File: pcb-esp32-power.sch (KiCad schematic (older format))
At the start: 15 parts, among them IC2 SY8008B, J1 C-OBD-II-16M, J2 Conn_01x02, J3 Bus_Connector, U1 STEPDOWN12_5

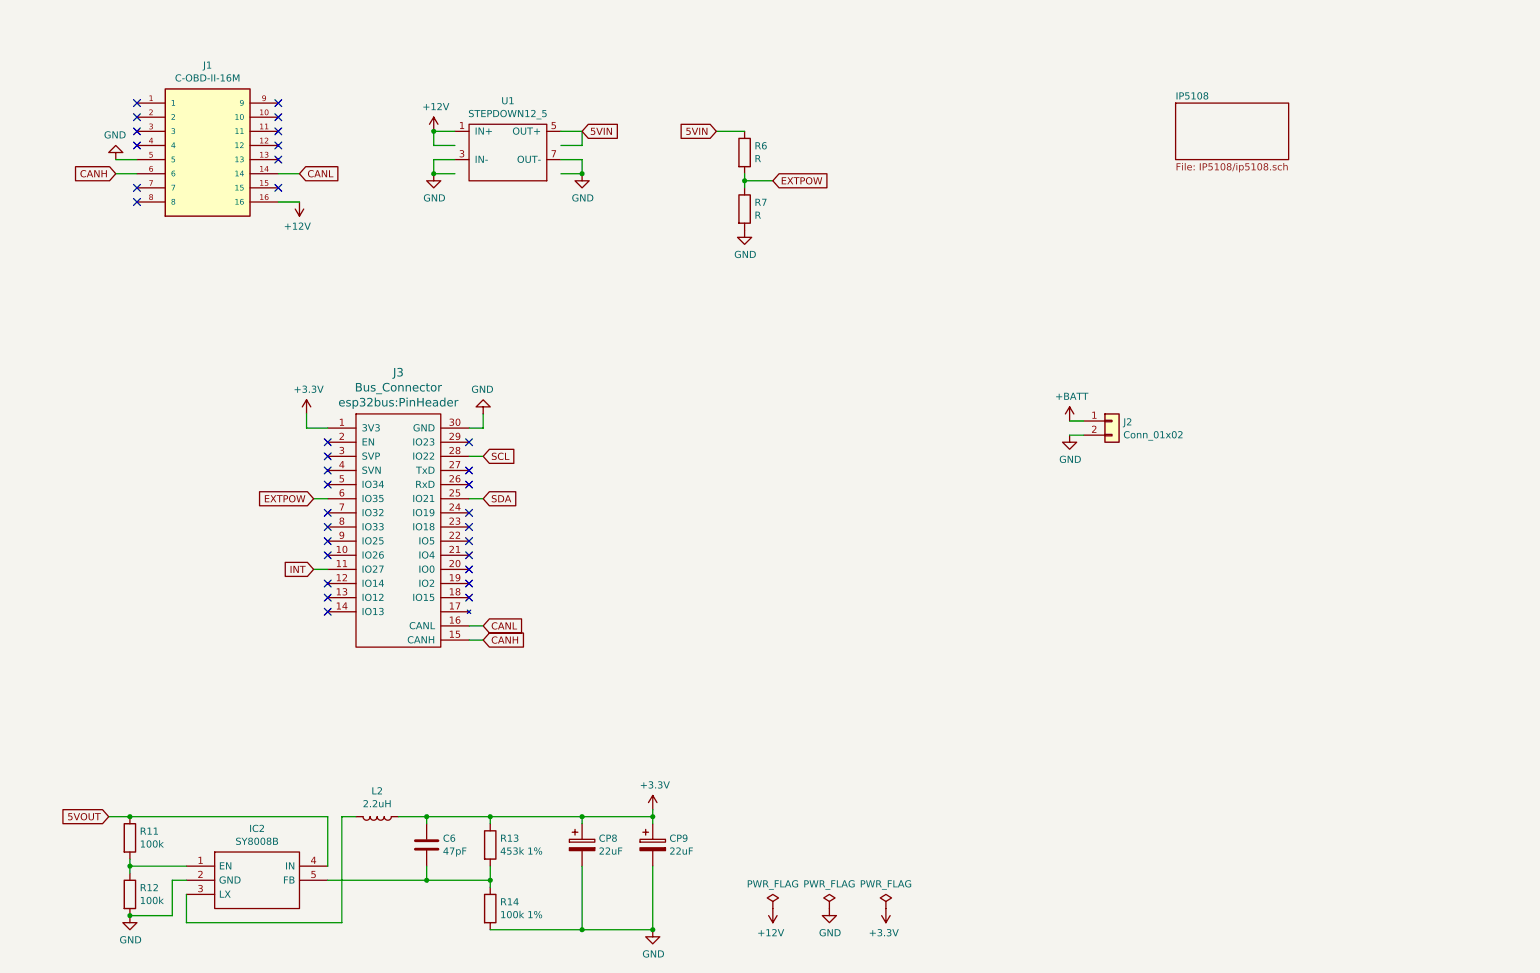
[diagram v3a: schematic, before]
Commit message: Umstellung auf TP4054/SY8008/LTC3440
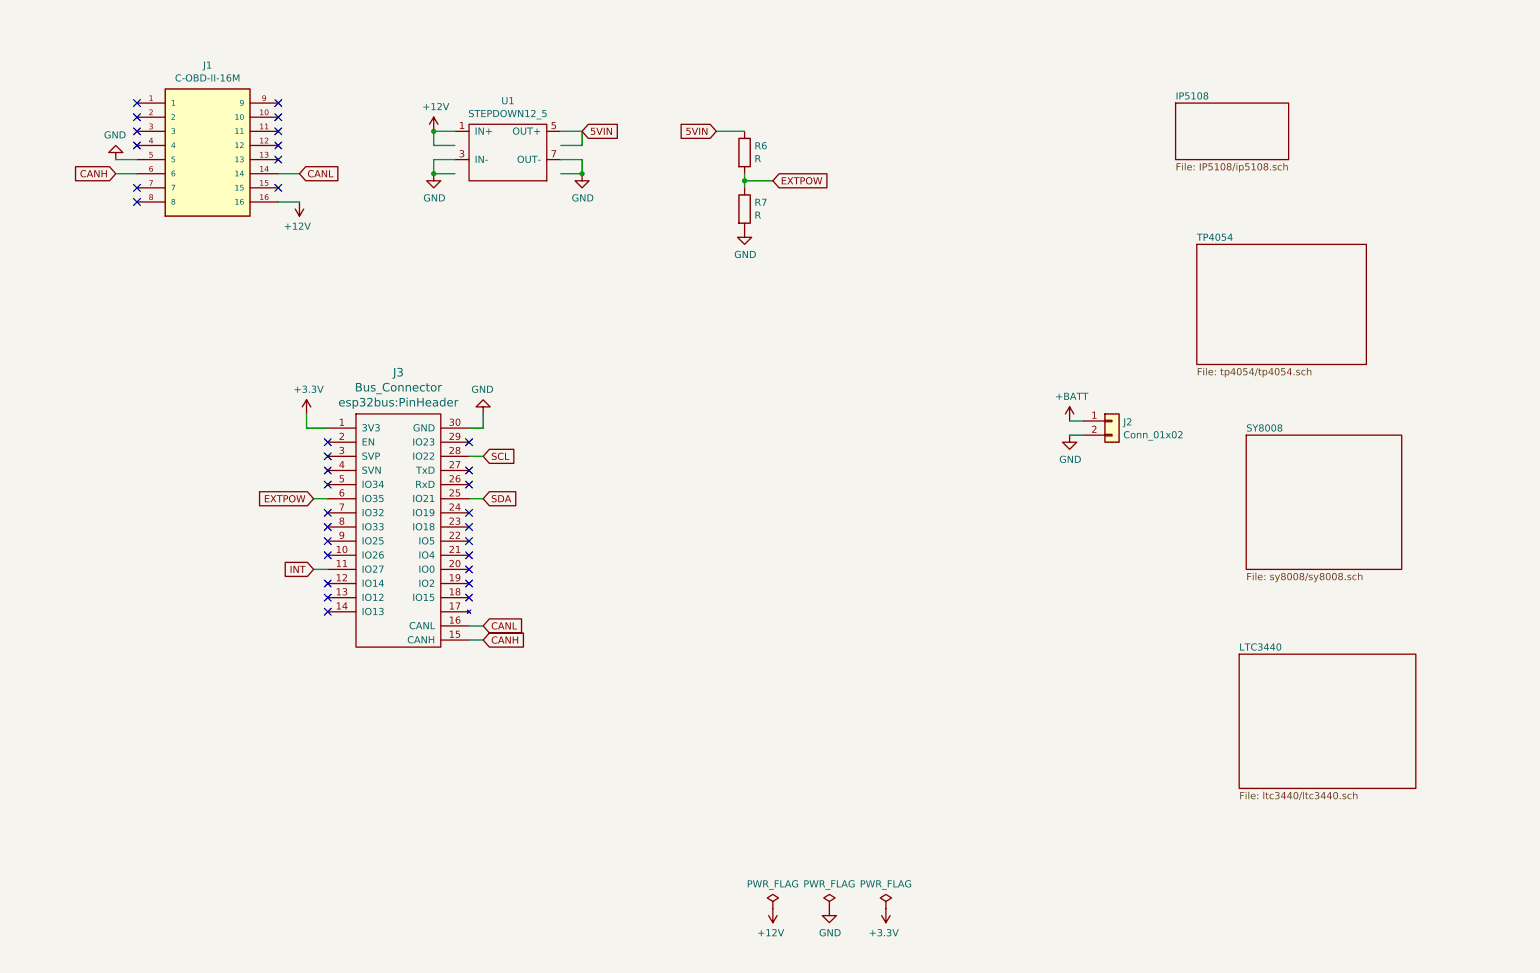
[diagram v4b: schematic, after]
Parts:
- removed C6: 47pF, Capacitor_SMD:C_0603_1608Metric_Pad1.08x0.95mm_HandSolder, symbol Device:C
- removed CP8, CP9: 22uF, Capacitor_Tantalum_SMD:CP_EIA-6032-28_Kemet-C_Pad2.25x2.35mm_HandSolder, symbol Device:CP
- removed IC2: SY8008B, SamacSys_Parts:SOT95P285X140-5N, symbol SamacSys_Parts:SY8008B
- removed L2: 2.2uH, IP5108:CD54_Inductor, symbol Device:L
- removed R11, R12: 100k, Resistor_SMD:R_0603_1608Metric_Pad0.98x0.95mm_HandSolder, symbol Device:R
- removed R13: 453k 1%, Resistor_SMD:R_0603_1608Metric_Pad0.98x0.95mm_HandSolder, symbol Device:R
- removed R14: 100k 1%, Resistor_SMD:R_0603_1608Metric_Pad0.98x0.95mm_HandSolder, symbol Device:R
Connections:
- net labels removed: 5VOUT
- wire segments 63 -> 32
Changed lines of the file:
@@
 $Descr A4 11693 8268
 encoding utf-8
-Sheet 1 2
+Sheet 1 5
 Title ""
 Date ""
@@
 $EndComp
 $Comp
-L SamacSys_Parts:SY8008B IC2
-U 1 1 60D71E94
-P 1600 6600
-F 0 "IC2" H 2100 6865 50  0000 C CNN
-F 1 "SY8008B" H 2100 6774 50  0000 C CNN
-F 2 "SamacSys_Parts:SOT95P285X140-5N" H 2450 6700 50  0001 L CNN
-F 3 "http://www.sunnyqi.com/upLoad/product/month_1306/SY8008.pdf" H 2450 6600 50  0001 L CNN
-F 4 "High Efficiency 1.5MHz, 0.6A/1A/1.2A Synchronous Step Down Regulator Preliminary Spec" H 2450 6500 50  0001 L CNN "Description"
-F 5 "1.4" H 2450 6400 50  0001 L CNN "Height"
-F 6 "Silergy" H 2450 6300 50  0001 L CNN "Manufacturer_Name"
-F 7 "SY8008B" H 2450 6200 50  0001 L CNN "Manufacturer_Part_Number"
-F 8 "" H 2450 6100 50  0001 L CNN "Mouser Part Number"
-F 9 "" H 2450 6000 50  0001 L CNN "Mouser Price/Stock"
-F 10 "" H 2450 5900 50  0001 L CNN "Arrow Part Number"
-F 11 "" H 2450 5800 50  0001 L CNN "Arrow Price/Stock"
-	1    1600 6600
-	1    0    0    -1
-$EndComp
-Text GLabel 1050 6250 0    50   Input ~ 0
-5VOUT
-$Comp
-L power:+3.3V #PWR0113
-U 1 1 60D73F07
-P 4900 6200
-F 0 "#PWR0113" H 4900 6050 50  0001 C CNN
-F 1 "+3.3V" H 4915 6373 50  0000 C CNN
-F 2 "" H 4900 6200 50  0001 C CNN
-F 3 "" H 4900 6200 50  0001 C CNN
-	1    4900 6200
-	1    0    0    -1
-$EndComp
-$Comp
 L power:PWR_FLAG #FLG0103
 U 1 1 60D74F1F
@@
 	-1   0    0    1
 $EndComp
-Wire Wire Line
-	2600 6600 2600 6250
-Wire Wire Line
-	2800 6250 2700 6250
-$Comp
-L Device:R R11
-U 1 1 60D79945
-P 1200 6400
-F 0 "R11" H 1270 6446 50  0000 L CNN
-F 1 "100k" H 1270 6355 50  0000 L CNN
-F 2 "Resistor_SMD:R_0603_1608Metric_Pad0.98x0.95mm_HandSolder" V 1130 6400 50  0001 C CNN
-F 3 "~" H 1200 6400 50  0001 C CNN
-	1    1200 6400
-	1    0    0    -1
-$EndComp
-$Comp
-L Device:R R12
-U 1 1 60D7A4DC
-P 1200 6800
-F 0 "R12" H 1270 6846 50  0000 L CNN
-F 1 "100k" H 1270 6755 50  0000 L CNN
-F 2 "Resistor_SMD:R_0603_1608Metric_Pad0.98x0.95mm_HandSolder" V 1130 6800 50  0001 C CNN
-F 3 "~" H 1200 6800 50  0001 C CNN
-	1    1200 6800
-	1    0    0    -1
-$EndComp
-Wire Wire Line
-	1200 6250 1050 6250
-$Comp
-L power:GND #PWR0115
-U 1 1 60D90272
-P 1200 6950
-F 0 "#PWR0115" H 1200 6700 50  0001 C CNN
-F 1 "GND" H 1205 6777 50  0000 C CNN
-F 2 "" H 1200 6950 50  0001 C CNN
-F 3 "" H 1200 6950 50  0001 C CNN
-	1    1200 6950
-	1    0    0    -1
-$EndComp
-$Comp
-L Device:L L2
-U 1 1 60DAEADC
-P 2950 6250
-F 0 "L2" V 2769 6250 50  0000 C CNN
-F 1 "2.2uH" V 2860 6250 50  0000 C CNN
-F 2 "IP5108:CD54_Inductor" H 2950 6250 50  0001 C CNN
-F 3 "~" H 2950 6250 50  0001 C CNN
-	1    2950 6250
-	0    1    1    0
-$EndComp
-$Comp
-L Device:C C6
-U 1 1 60DAFF2B
-P 3300 6450
-F 0 "C6" H 3415 6496 50  0000 L CNN
-F 1 "47pF" H 3415 6405 50  0000 L CNN
-F 2 "Capacitor_SMD:C_0603_1608Metric_Pad1.08x0.95mm_HandSolder" H 3338 6300 50  0001 C CNN
-F 3 "~" H 3300 6450 50  0001 C CNN
-	1    3300 6450
-	1    0    0    -1
-$EndComp
-$Comp
-L Device:R R13
-U 1 1 60DB5688
-P 3750 6450
-F 0 "R13" H 3820 6496 50  0000 L CNN
-F 1 "453k 1%" H 3820 6405 50  0000 L CNN
-F 2 "Resistor_SMD:R_0603_1608Metric_Pad0.98x0.95mm_HandSolder" V 3680 6450 50  0001 C CNN
-F 3 "~" H 3750 6450 50  0001 C CNN
-	1    3750 6450
-	1    0    0    -1
-$EndComp
-$Comp
-L Device:R R14
-U 1 1 60DB5D90
-P 3750 6900
-F 0 "R14" H 3820 6946 50  0000 L CNN
-F 1 "100k 1%" H 3820 6855 50  0000 L CNN
-F 2 "Resistor_SMD:R_0603_1608Metric_Pad0.98x0.95mm_HandSolder" V 3680 6900 50  0001 C CNN
-F 3 "~" H 3750 6900 50  0001 C CNN
-	1    3750 6900
-	1    0    0    -1
-$EndComp
-$Comp
-L Device:CP CP8
-U 1 1 60DB6F82
-P 4400 6450
-F 0 "CP8" H 4518 6496 50  0000 L CNN
-F 1 "22uF" H 4518 6405 50  0000 L CNN
-F 2 "Capacitor_Tantalum_SMD:CP_EIA-6032-28_Kemet-C_Pad2.25x2.35mm_HandSolder" H 4438 6300 50  0001 C CNN
-F 3 "~" H 4400 6450 50  0001 C CNN
-	1    4400 6450
-	1    0    0    -1
-$EndComp
-$Comp
-L Device:CP CP9
-U 1 1 60DB78E9
-P 4900 6450
-F 0 "CP9" H 5018 6496 50  0000 L CNN
-F 1 "22uF" H 5018 6405 50  0000 L CNN
-F 2 "Capacitor_Tantalum_SMD:CP_EIA-6032-28_Kemet-C_Pad2.25x2.35mm_HandSolder" H 4938 6300 50  0001 C CNN
-F 3 "~" H 4900 6450 50  0001 C CNN
-	1    4900 6450
-	1    0    0    -1
-$EndComp
-Wire Wire Line
-	3100 6250 3300 6250
-Wire Wire Line
-	4900 6250 4900 6200
-Wire Wire Line
-	3300 6300 3300 6250
-Connection ~ 3300 6250
-Wire Wire Line
-	3300 6250 3750 6250
-Wire Wire Line
-	3750 6300 3750 6250
-Connection ~ 3750 6250
-Wire Wire Line
-	3750 6250 4400 6250
-Wire Wire Line
-	4400 6300 4400 6250
-Connection ~ 4400 6250
-Wire Wire Line
-	4400 6250 4900 6250
-Wire Wire Line
-	4900 6300 4900 6250
-Connection ~ 4900 6250
-Wire Wire Line
-	2600 6700 3300 6700
-Wire Wire Line
-	3750 6700 3750 6600
-Wire Wire Line
-	3300 6600 3300 6700
-Connection ~ 3300 6700
-Wire Wire Line
-	3300 6700 3750 6700
-Wire Wire Line
-	3750 6750 3750 6700
-Connection ~ 3750 6700
-Wire Wire Line
-	4900 6600 4900 7050
-Wire Wire Line
-	4900 7050 4400 7050
-Wire Wire Line
-	4400 6600 4400 7050
-Connection ~ 4400 7050
-Wire Wire Line
-	4400 7050 3750 7050
-$Comp
-L power:GND #PWR0116
-U 1 1 60DDFC8D
-P 4900 7050
-F 0 "#PWR0116" H 4900 6800 50  0001 C CNN
-F 1 "GND" H 4905 6877 50  0000 C CNN
-F 2 "" H 4900 7050 50  0001 C CNN
-F 3 "" H 4900 7050 50  0001 C CNN
-	1    4900 7050
-	1    0    0    -1
-$EndComp
-Connection ~ 4900 7050
-Wire Wire Line
-	1600 6800 1600 7000
-Wire Wire Line
-	1600 7000 2700 7000
-Wire Wire Line
-	2700 7000 2700 6250
-Wire Wire Line
-	2600 6250 1200 6250
-Connection ~ 1200 6250
-Wire Wire Line
-	1600 6600 1200 6600
-Wire Wire Line
-	1200 6600 1200 6550
-Wire Wire Line
-	1200 6650 1200 6600
-Connection ~ 1200 6600
-Wire Wire Line
-	1600 6700 1500 6700
-Wire Wire Line
-	1500 6700 1500 6950
-Wire Wire Line
-	1500 6950 1200 6950
-Connection ~ 1200 6950
 $Comp
 L Connector_Generic:Conn_01x02 J2
@@
 NoConn ~ 2250 1300
 NoConn ~ 2250 1200
+$Sheet
+S 8750 2200 1200 850
+U 612652A3
+F0 "TP4054" 50
+F1 "tp4054/tp4054.sch" 50
+$EndSheet
+$Sheet
+S 9100 3550 1100 950
+U 612B5E8A
+F0 "SY8008" 50
+F1 "sy8008/sy8008.sch" 50
+$EndSheet
+$Sheet
+S 9050 5100 1250 950
+U 612C7D18
+F0 "LTC3440" 50
+F1 "ltc3440/ltc3440.sch" 50
+$EndSheet
 $EndSCHEMATC

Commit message: LTC3530 eingefügt
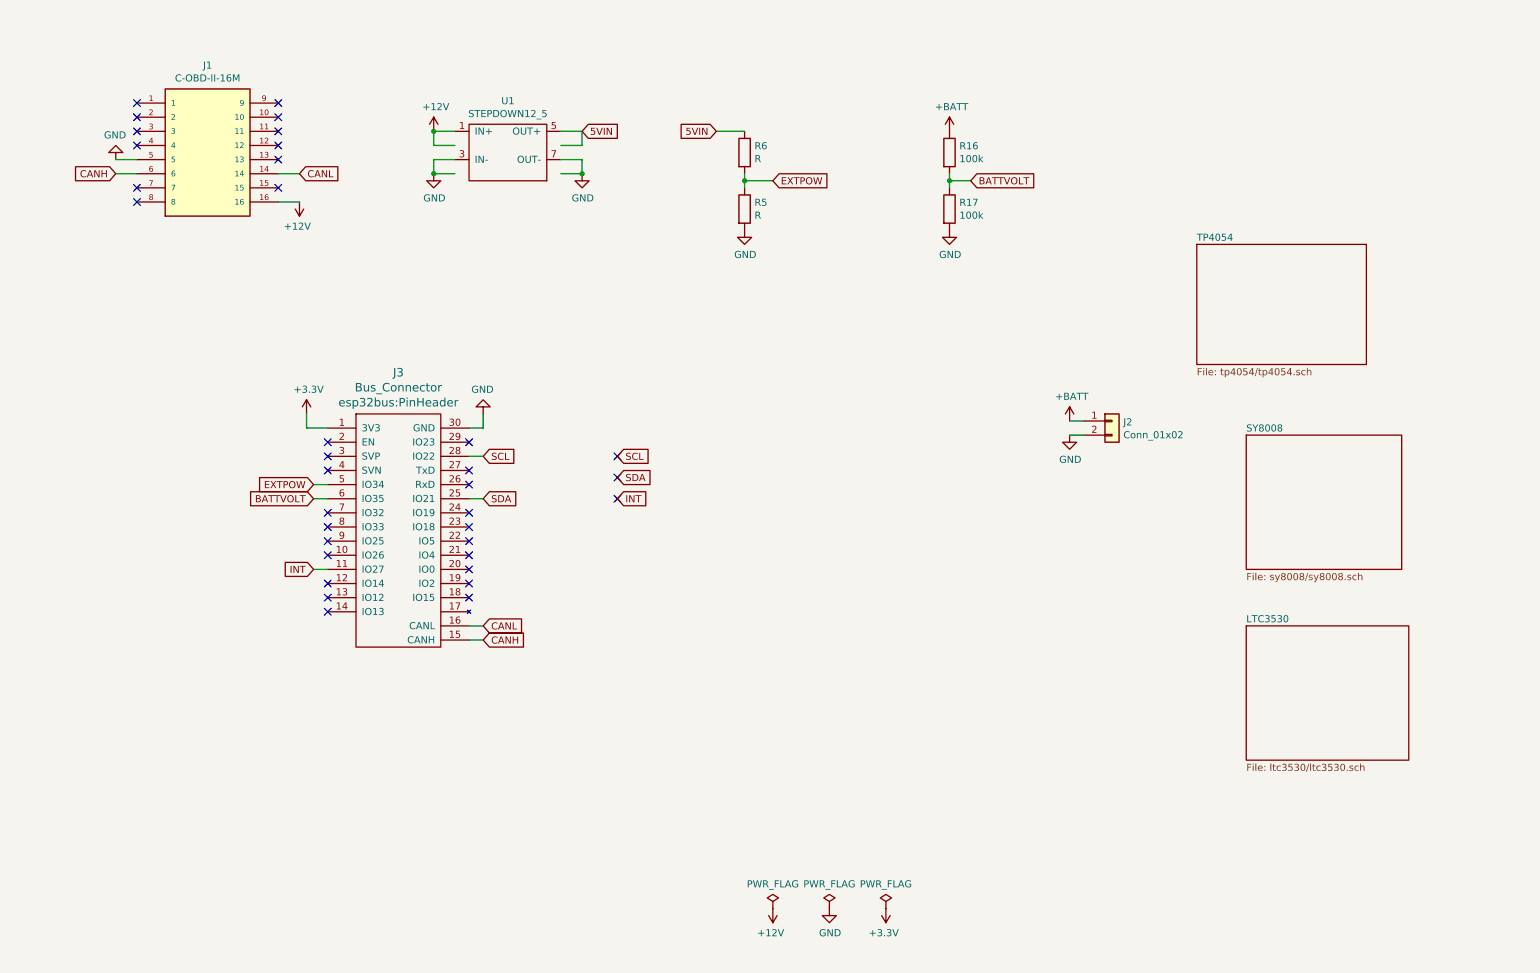
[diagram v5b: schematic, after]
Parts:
- added R16, R17: 100k, Resistor_SMD:R_0603_1608Metric_Pad0.98x0.95mm_HandSolder, symbol Device:R
- renumbered R7 to R5
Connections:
- net labels added: BATTVOLT
- wire segments 32 -> 36
- no-connect marks 33 -> 35
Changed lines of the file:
@@
 $Descr A4 11693 8268
 encoding utf-8
-Sheet 1 5
+Sheet 1 4
 Title ""
 Date ""
@@
 	1    0    0    -1
 $EndComp
-$Sheet
-S 8600 1200 800  400
-U 60F1A96E
-F0 "IP5108" 50
-F1 "IP5108/ip5108.sch" 50
-$EndSheet
 $Comp
 L power:+BATT #PWR0101
@@
 $EndComp
 $Comp
-L Device:R R7
+L Device:R R5
 U 1 1 60F61A44
 P 5550 1950
-F 0 "R7" H 5620 1996 50  0000 L CNN
+F 0 "R5" H 5620 1996 50  0000 L CNN
 F 1 "R" H 5620 1905 50  0000 L CNN
 F 2 "Resistor_SMD:R_0603_1608Metric_Pad0.98x0.95mm_HandSolder" V 5480 1950 50  0001 C CNN
@@
 	1    0    0    -1
 $EndComp
-Text GLabel 2500 4000 0    50   Input ~ 0
+Text GLabel 2500 3900 0    50   Input ~ 0
 EXTPOW
 Text GLabel 3700 4000 2    50   Input ~ 0
@@
 NoConn ~ 2600 3700
 NoConn ~ 2600 3800
-NoConn ~ 2600 3900
 NoConn ~ 2600 4100
 NoConn ~ 2600 4200
@@
 $EndSheet
 $Sheet
-S 9050 5100 1250 950
-U 612C7D18
-F0 "LTC3440" 50
-F1 "ltc3440/ltc3440.sch" 50
+S 9100 4900 1150 950
+U 612FA5D2
+F0 "LTC3530" 50
+F1 "ltc3530/ltc3530.sch" 50
 $EndSheet
+Wire Wire Line
+	2500 3900 2600 3900
+Text GLabel 2500 4000 0    50   Input ~ 0
+BATTVOLT
+Text GLabel 7150 1750 2    50   Input ~ 0
+BATTVOLT
+$Comp
+L power:+BATT #PWR0116
+U 1 1 6131DA4C
+P 7000 1400
+F 0 "#PWR0116" H 7000 1250 50  0001 C CNN
+F 1 "+BATT" H 7015 1573 50  0000 C CNN
+F 2 "" H 7000 1400 50  0001 C CNN
+F 3 "" H 7000 1400 50  0001 C CNN
+	1    7000 1400
+	1    0    0    -1
+$EndComp
+$Comp
+L Device:R R16
+U 1 1 6131E154
+P 7000 1550
+F 0 "R16" H 7070 1596 50  0000 L CNN
+F 1 "100k" H 7070 1505 50  0000 L CNN
+F 2 "Resistor_SMD:R_0603_1608Metric_Pad0.98x0.95mm_HandSolder" V 6930 1550 50  0001 C CNN
+F 3 "~" H 7000 1550 50  0001 C CNN
+	1    7000 1550
+	1    0    0    -1
+$EndComp
+$Comp
+L Device:R R17
+U 1 1 6131E8A9
+P 7000 1950
+F 0 "R17" H 7070 1996 50  0000 L CNN
+F 1 "100k" H 7070 1905 50  0000 L CNN
+F 2 "Resistor_SMD:R_0603_1608Metric_Pad0.98x0.95mm_HandSolder" V 6930 1950 50  0001 C CNN
+F 3 "~" H 7000 1950 50  0001 C CNN
+	1    7000 1950
+	1    0    0    -1
+$EndComp
+$Comp
+L power:GND #PWR0117
+U 1 1 6131ED93
+P 7000 2100
+F 0 "#PWR0117" H 7000 1850 50  0001 C CNN
+F 1 "GND" H 7005 1927 50  0000 C CNN
+F 2 "" H 7000 2100 50  0001 C CNN
+F 3 "" H 7000 2100 50  0001 C CNN
+	1    7000 2100
+	1    0    0    -1
+$EndComp
+Wire Wire Line
+	7000 1700 7000 1750
+Wire Wire Line
+	7150 1750 7000 1750
+Connection ~ 7000 1750
+Wire Wire Line
+	7000 1750 7000 1800
+Text GLabel 4650 3700 2    50   Input ~ 0
+SCL
+Text GLabel 4650 3850 2    50   Input ~ 0
+SDA
+Text GLabel 4650 4000 2    50   Input ~ 0
+INT
+NoConn ~ 4650 3700
+NoConn ~ 4650 3850
+NoConn ~ 4650 4000
 $EndSCHEMATC
